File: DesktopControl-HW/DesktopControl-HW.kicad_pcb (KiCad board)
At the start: 4 copper layers, 180 x 80 mm, 64 parts, among them IC401 OPA172IDBVT, IC402 OPA172IDBVT, IC403 OPA172IDBVT, IC404 TLV1701AIDCKT, IC501 OPA172IDBVT, IC502 OPA172IDBVT, IC503 OPA172IDBVT, IC504 TLV1701AIDCKT, U201 PCM2902, Y201 LFXTAL035264

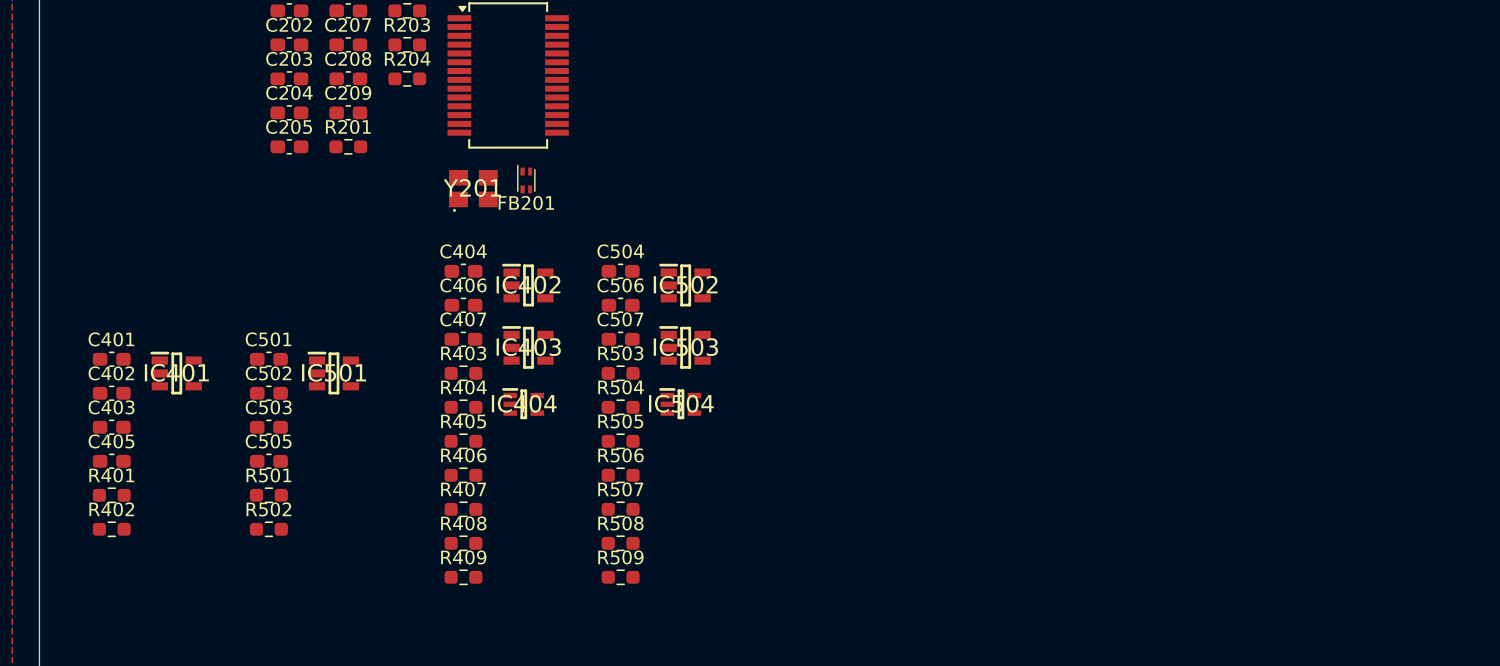
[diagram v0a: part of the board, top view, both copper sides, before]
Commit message: Rework amplifier configuration, add amplifier for subwoofer and start check of codec
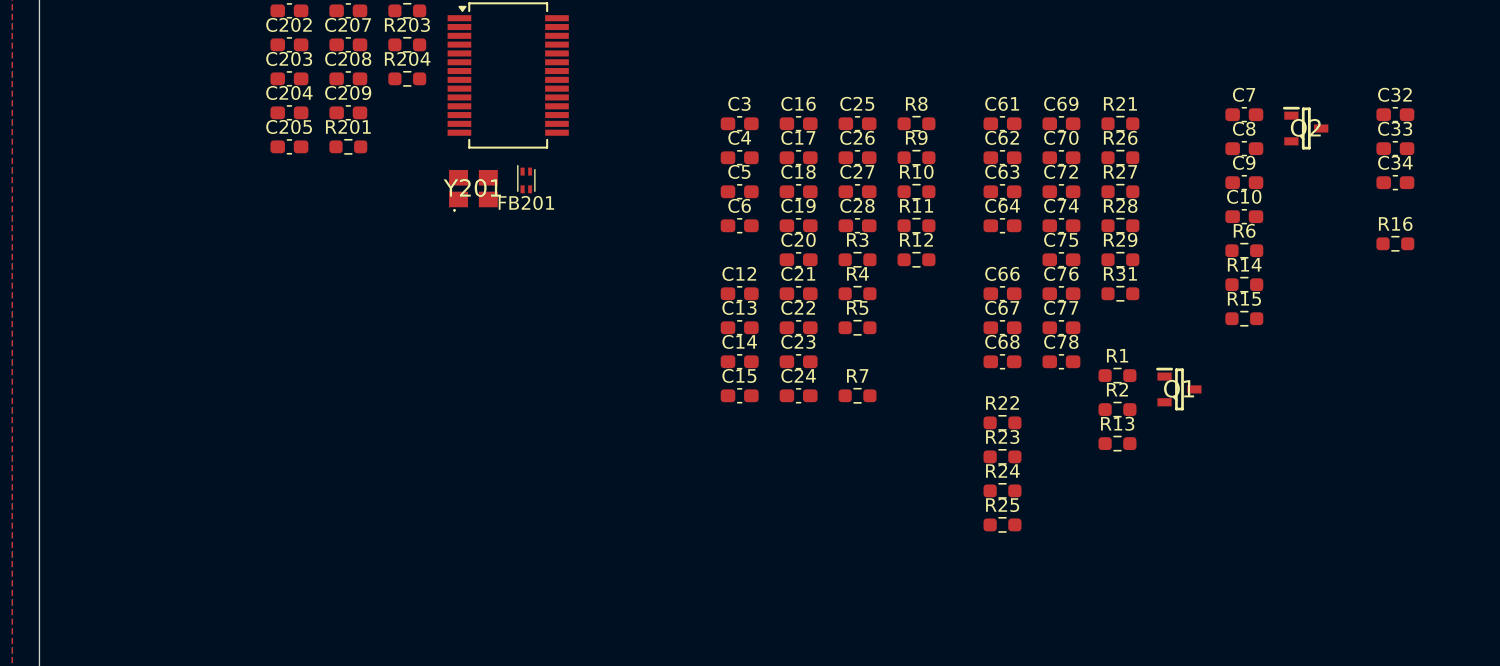
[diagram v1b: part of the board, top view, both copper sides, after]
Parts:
- removed C401, C402, C403, C405, C406, C407, C501, C502, C503, C505, C506, C507: C, Capacitor_SMD:C_0603_1608Metric_Pad1.08x0.95mm_HandSolder
- removed C404, C504: 470n, Capacitor_SMD:C_0603_1608Metric_Pad1.08x0.95mm_HandSolder
- removed IC401, IC402, IC403, IC501, IC502, IC503: OPA172IDBVT, Lund Formula Student:SOT95P280X145-5N
- removed IC404, IC504: TLV1701AIDCKT, Lund Formula Student:SOT65P210X110-5N
- removed R401, R402, R404, R501, R502, R504: 1M, Resistor_SMD:R_0603_1608Metric_Pad0.98x0.95mm_HandSolder
- removed R403, R503: 18k, Resistor_SMD:R_0603_1608Metric_Pad0.98x0.95mm_HandSolder
- removed R405, R505: 22R, Resistor_SMD:R_0603_1608Metric_Pad0.98x0.95mm_HandSolder
- removed R406, R409, R506, R509: TBD, Resistor_SMD:R_0603_1608Metric_Pad0.98x0.95mm_HandSolder
- removed R407, R408, R507, R508: 0R, Resistor_SMD:R_0603_1608Metric_Pad0.98x0.95mm_HandSolder
- added C10: 1u, Capacitor_SMD:C_0603_1608Metric_Pad1.08x0.95mm_HandSolder, F.Cu at (128.9, 72.8)
- added C12: C, Capacitor_SMD:C_0603_1608Metric_Pad1.08x0.95mm_HandSolder, F.Cu at (91.7, 78.4)
- added C13: 220n, Capacitor_SMD:C_0603_1608Metric_Pad1.08x0.95mm_HandSolder, F.Cu at (91.7, 81.0)
- added C14: 220n, Capacitor_SMD:C_0603_1608Metric_Pad1.08x0.95mm_HandSolder, F.Cu at (91.7, 83.5)
- added C15: 220n, Capacitor_SMD:C_0603_1608Metric_Pad1.08x0.95mm_HandSolder, F.Cu at (91.7, 86.0)
- added C16: 220n, Capacitor_SMD:C_0603_1608Metric_Pad1.08x0.95mm_HandSolder, F.Cu at (96.0, 65.9)
- added C17: 680n, Capacitor_SMD:C_0603_1608Metric_Pad1.08x0.95mm_HandSolder, F.Cu at (96.0, 68.4)
- added C18: 680n, Capacitor_SMD:C_0603_1608Metric_Pad1.08x0.95mm_HandSolder, F.Cu at (96.0, 70.9)
- added C19: 1n, Capacitor_SMD:C_0603_1608Metric_Pad1.08x0.95mm_HandSolder, F.Cu at (96.0, 73.4)
- added C20: 1n, Capacitor_SMD:C_0603_1608Metric_Pad1.08x0.95mm_HandSolder, F.Cu at (96.0, 75.9)
- added C21: 10n, Capacitor_SMD:C_0603_1608Metric_Pad1.08x0.95mm_HandSolder, F.Cu at (96.0, 78.4)
- added C22: 10n, Capacitor_SMD:C_0603_1608Metric_Pad1.08x0.95mm_HandSolder, F.Cu at (96.0, 81.0)
- added C23: 1n, Capacitor_SMD:C_0603_1608Metric_Pad1.08x0.95mm_HandSolder, F.Cu at (96.0, 83.5)
- added C24: 680n, Capacitor_SMD:C_0603_1608Metric_Pad1.08x0.95mm_HandSolder, F.Cu at (96.0, 86.0)
- added C25: 10n, Capacitor_SMD:C_0603_1608Metric_Pad1.08x0.95mm_HandSolder, F.Cu at (100.4, 65.9)
- added C26: 680n, Capacitor_SMD:C_0603_1608Metric_Pad1.08x0.95mm_HandSolder, F.Cu at (100.4, 68.4)
- added C27: 10n, Capacitor_SMD:C_0603_1608Metric_Pad1.08x0.95mm_HandSolder, F.Cu at (100.4, 70.9)
- added C28: 1n, Capacitor_SMD:C_0603_1608Metric_Pad1.08x0.95mm_HandSolder, F.Cu at (100.4, 73.4)
- added C3: 100n, Capacitor_SMD:C_0603_1608Metric_Pad1.08x0.95mm_HandSolder, F.Cu at (91.7, 65.9)
- added C32: 1u, Capacitor_SMD:C_0603_1608Metric_Pad1.08x0.95mm_HandSolder, F.Cu at (140.1, 65.2)
- added C33: 1u, Capacitor_SMD:C_0603_1608Metric_Pad1.08x0.95mm_HandSolder, F.Cu at (140.1, 67.7)
- added C34: 1u, Capacitor_SMD:C_0603_1608Metric_Pad1.08x0.95mm_HandSolder, F.Cu at (140.1, 70.2)
- added C4: 100n, Capacitor_SMD:C_0603_1608Metric_Pad1.08x0.95mm_HandSolder, F.Cu at (91.7, 68.4)
- added C5: 1n, Capacitor_SMD:C_0603_1608Metric_Pad1.08x0.95mm_HandSolder, F.Cu at (91.7, 70.9)
- added C6: 1n, Capacitor_SMD:C_0603_1608Metric_Pad1.08x0.95mm_HandSolder, F.Cu at (91.7, 73.4)
- added C61: 100n, Capacitor_SMD:C_0603_1608Metric_Pad1.08x0.95mm_HandSolder, F.Cu at (111.1, 65.9)
- added C62: 100n, Capacitor_SMD:C_0603_1608Metric_Pad1.08x0.95mm_HandSolder, F.Cu at (111.1, 68.4)
- added C63: 1n, Capacitor_SMD:C_0603_1608Metric_Pad1.08x0.95mm_HandSolder, F.Cu at (111.1, 70.9)
- added C64: 1n, Capacitor_SMD:C_0603_1608Metric_Pad1.08x0.95mm_HandSolder, F.Cu at (111.1, 73.4)
- added C66: 220n, Capacitor_SMD:C_0603_1608Metric_Pad1.08x0.95mm_HandSolder, F.Cu at (111.1, 78.4)
- added C67: 220n, Capacitor_SMD:C_0603_1608Metric_Pad1.08x0.95mm_HandSolder, F.Cu at (111.1, 81.0)
- added C68: 1u, Capacitor_SMD:C_0603_1608Metric_Pad1.08x0.95mm_HandSolder, F.Cu at (111.1, 83.5)
- added C69: 680n, Capacitor_SMD:C_0603_1608Metric_Pad1.08x0.95mm_HandSolder, F.Cu at (115.4, 65.9)
- added C7: 1u, Capacitor_SMD:C_0603_1608Metric_Pad1.08x0.95mm_HandSolder, F.Cu at (128.9, 65.2)
- added C70: 10n, Capacitor_SMD:C_0603_1608Metric_Pad1.08x0.95mm_HandSolder, F.Cu at (115.4, 68.4)
- added C72: 220n, Capacitor_SMD:C_0603_1608Metric_Pad1.08x0.95mm_HandSolder, F.Cu at (115.4, 70.9)
- added C74: 680n, Capacitor_SMD:C_0603_1608Metric_Pad1.08x0.95mm_HandSolder, F.Cu at (115.4, 73.4)
- added C75: 10n, Capacitor_SMD:C_0603_1608Metric_Pad1.08x0.95mm_HandSolder, F.Cu at (115.4, 75.9)
- added C76: 220n, Capacitor_SMD:C_0603_1608Metric_Pad1.08x0.95mm_HandSolder, F.Cu at (115.4, 78.4)
- added C77: 1u, Capacitor_SMD:C_0603_1608Metric_Pad1.08x0.95mm_HandSolder, F.Cu at (115.4, 81.0)
- added C78: 1u, Capacitor_SMD:C_0603_1608Metric_Pad1.08x0.95mm_HandSolder, F.Cu at (115.4, 83.5)
- added C8: 1u, Capacitor_SMD:C_0603_1608Metric_Pad1.08x0.95mm_HandSolder, F.Cu at (128.9, 67.7)
- added C9: 1u, Capacitor_SMD:C_0603_1608Metric_Pad1.08x0.95mm_HandSolder, F.Cu at (128.9, 70.2)
- added Q1: PMV280ENEAR, Lund Formula Student:SOT95P230X110-3N, F.Cu at (124.2, 85.5)
- added Q2: PMV280ENEAR, Lund Formula Student:SOT95P230X110-3N, F.Cu at (133.5, 66.2)
- added R1: 100k, Resistor_SMD:R_0603_1608Metric_Pad0.98x0.95mm_HandSolder, F.Cu at (119.6, 84.5)
- added R10: 3R3, Resistor_SMD:R_0603_1608Metric_Pad0.98x0.95mm_HandSolder, F.Cu at (104.7, 70.9)
- added R11: 47k, Resistor_SMD:R_0603_1608Metric_Pad0.98x0.95mm_HandSolder, F.Cu at (104.7, 73.4)
- added R12: 47k, Resistor_SMD:R_0603_1608Metric_Pad0.98x0.95mm_HandSolder, F.Cu at (104.7, 75.9)
- added R13: 10k, Resistor_SMD:R_0603_1608Metric_Pad0.98x0.95mm_HandSolder, F.Cu at (119.6, 89.5)
- added R14: 10k, Resistor_SMD:R_0603_1608Metric_Pad0.98x0.95mm_HandSolder, F.Cu at (128.9, 77.8)
- added R15: 100k, Resistor_SMD:R_0603_1608Metric_Pad0.98x0.95mm_HandSolder, F.Cu at (128.9, 80.3)
- added R16: 10k, Resistor_SMD:R_0603_1608Metric_Pad0.98x0.95mm_HandSolder, F.Cu at (140.1, 74.8)
- added R2: 10k, Resistor_SMD:R_0603_1608Metric_Pad0.98x0.95mm_HandSolder, F.Cu at (119.6, 87.0)
- added R21: 3R3, Resistor_SMD:R_0603_1608Metric_Pad0.98x0.95mm_HandSolder, F.Cu at (119.8, 65.9)
- added R22: 12k, Resistor_SMD:R_0603_1608Metric_Pad0.98x0.95mm_HandSolder, F.Cu at (111.1, 88.0)
- added R23: 12k, Resistor_SMD:R_0603_1608Metric_Pad0.98x0.95mm_HandSolder, F.Cu at (111.1, 90.5)
- added R24: 47k, Resistor_SMD:R_0603_1608Metric_Pad0.98x0.95mm_HandSolder, F.Cu at (111.1, 93.0)
- added R25: 47k, Resistor_SMD:R_0603_1608Metric_Pad0.98x0.95mm_HandSolder, F.Cu at (111.1, 95.5)
- added R26: 47k, Resistor_SMD:R_0603_1608Metric_Pad0.98x0.95mm_HandSolder, F.Cu at (119.8, 68.4)
- added R27: 3R3, Resistor_SMD:R_0603_1608Metric_Pad0.98x0.95mm_HandSolder, F.Cu at (119.8, 70.9)
- added R28: 51k, Resistor_SMD:R_0603_1608Metric_Pad0.98x0.95mm_HandSolder, F.Cu at (119.8, 73.4)
- added R29: 51k, Resistor_SMD:R_0603_1608Metric_Pad0.98x0.95mm_HandSolder, F.Cu at (119.8, 75.9)
- added R3: 47k, Resistor_SMD:R_0603_1608Metric_Pad0.98x0.95mm_HandSolder, F.Cu at (100.4, 75.9)
- added R31: 100k, Resistor_SMD:R_0603_1608Metric_Pad0.98x0.95mm_HandSolder, F.Cu at (119.8, 78.4)
- added R4: 5k6, Resistor_SMD:R_0603_1608Metric_Pad0.98x0.95mm_HandSolder, F.Cu at (100.4, 78.4)
- added R5: 10k, Resistor_SMD:R_0603_1608Metric_Pad0.98x0.95mm_HandSolder, F.Cu at (100.4, 81.0)
- added R6: 10k, Resistor_SMD:R_0603_1608Metric_Pad0.98x0.95mm_HandSolder, F.Cu at (128.9, 75.3)
- added R7: 3R3, Resistor_SMD:R_0603_1608Metric_Pad0.98x0.95mm_HandSolder, F.Cu at (100.4, 86.0)
- added R8: 3R3, Resistor_SMD:R_0603_1608Metric_Pad0.98x0.95mm_HandSolder, F.Cu at (104.7, 65.9)
- added R9: 3R3, Resistor_SMD:R_0603_1608Metric_Pad0.98x0.95mm_HandSolder, F.Cu at (104.7, 68.4)
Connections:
- U201 pad 15: /AMPLIFIER_R/AUDIO_IN -> /CODEC/AUDIO_R
- U201 pad 16: /AMPLIFIER_L/AUDIO_IN -> /CODEC/AUDIO_L
